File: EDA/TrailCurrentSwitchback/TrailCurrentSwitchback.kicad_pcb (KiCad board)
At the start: 2 copper layers, 25.4 x 51.8 mm, 5 parts, among them IC1 SN65HVD230DR, J1 Conn_01x20, J2 Conn_01x20, J3 S2B-XH-SM4-TB

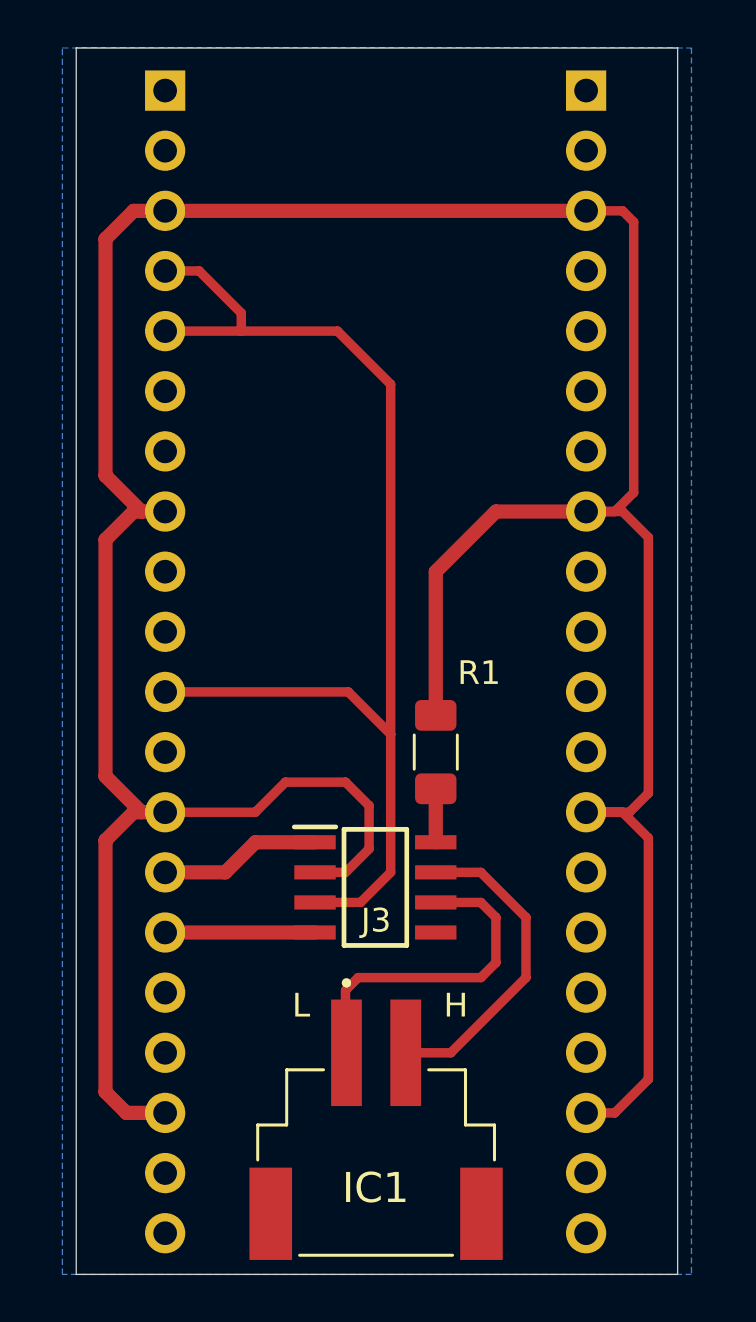
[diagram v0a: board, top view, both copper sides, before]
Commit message: Updated EDA for professional assembly. Gerber files added ordered 1.0.0 version of the PCB for testing.
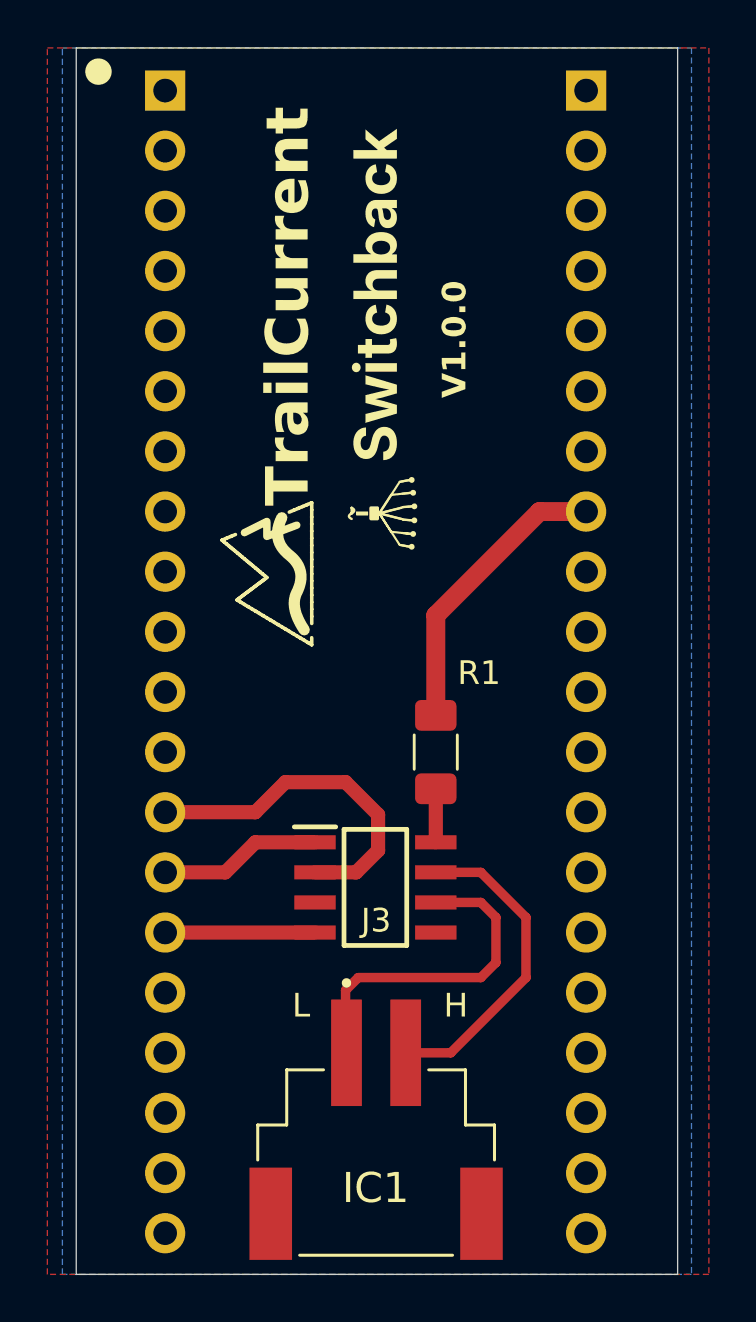
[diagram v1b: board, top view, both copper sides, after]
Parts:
- added LOGO: TrailCurrentLogo_Icon, TrailCurrentFootprints:TrailCurrentLogo_Icon, F.Cu at (131.3, 91.5)
- added LOGO: TrailCurrentLogo_Text, TrailCurrentFootprints:TrailCurrentLogo_Text, F.Cu at (154.4, 84.0)
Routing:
- net GND: track 143.5 -> 27.0 mm
- net +3.3V: track 49.8 -> 0.00 mm
- added copper zone on F.Cu, net +3.3V
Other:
- board text added: "V1.0.0"
